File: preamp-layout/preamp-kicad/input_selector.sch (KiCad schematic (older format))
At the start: 43 parts, among them J50 Conn_01x02_Female, J51 Conn_01x03_Male, J52 Conn_01x03_Male, J53 Conn_01x03_Male, J54 Conn_01x03_Male, J55 Conn_01x03_Male, J56 Conn_01x07_Female, J57 Conn_01x07_Female, J58 Conn_01x03_Male, J59 Conn_01x03_Female, J60 Conn_01x02_Male, J61 Conn_01x02_Male, J62 Conn_01x03_Female, J63 Conn_01x03_Female, K2 G6JU, K3 G6JU, K4 G6JU, K5 G6JU, K6 G6JU, K7 G6JU, K8 G6JU, U6 MCP23017_SO, U7 ULN2003, U8 ULN2003

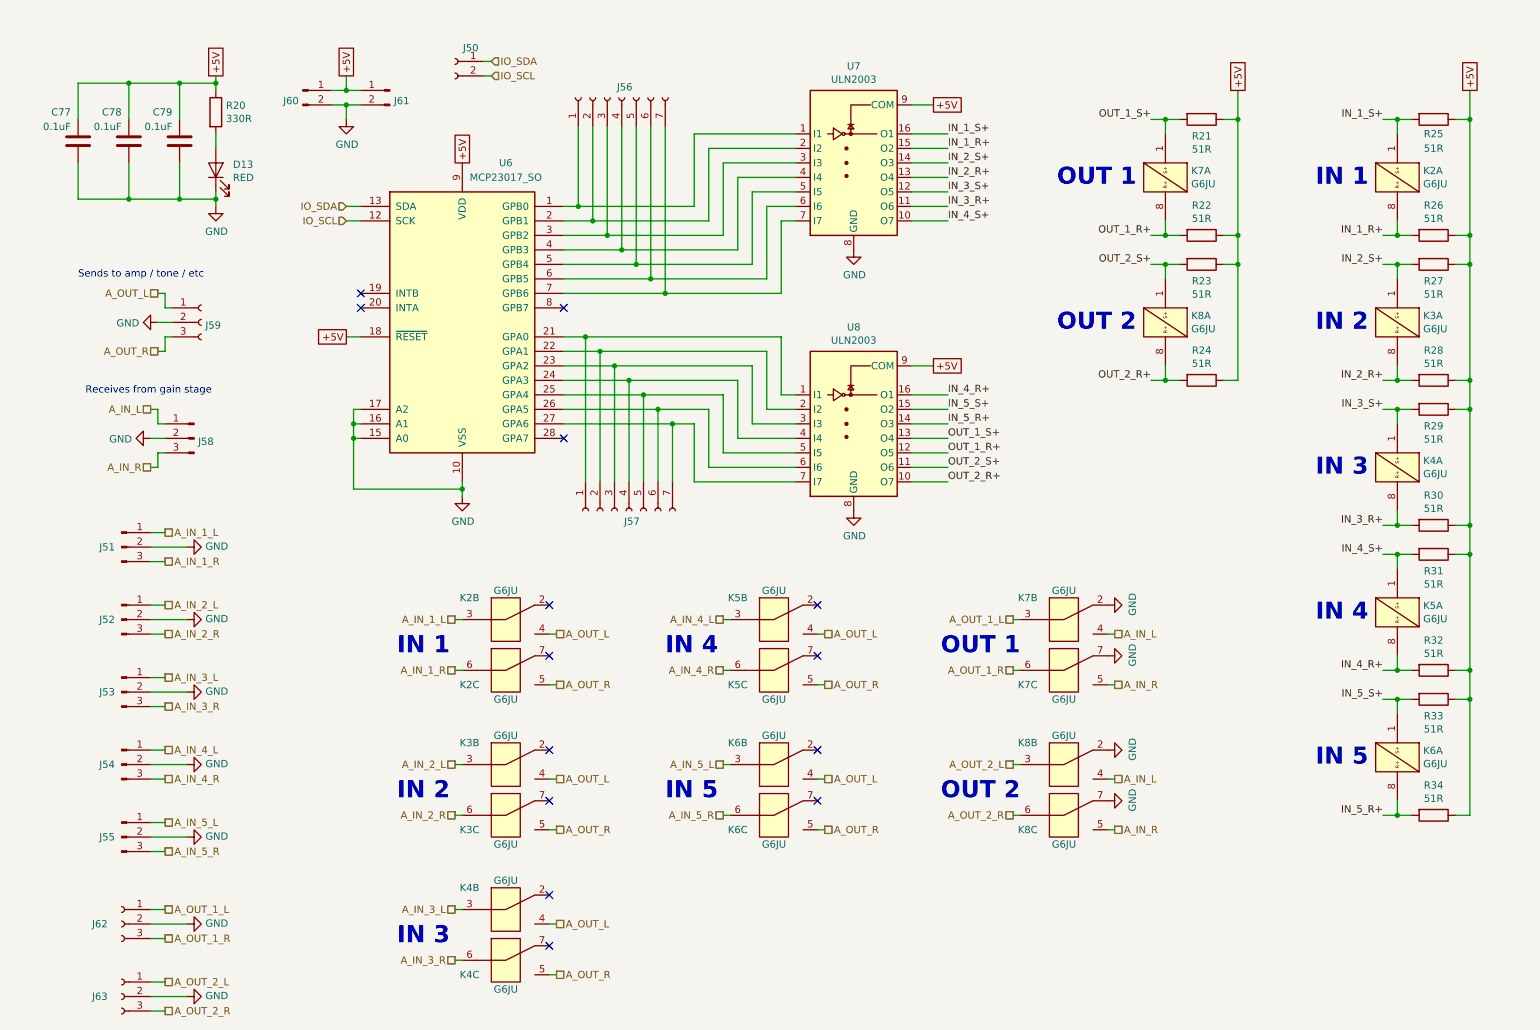
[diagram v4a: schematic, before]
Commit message: RefDes Update
Re-ran refdes assignment, updated BOM accordingly.
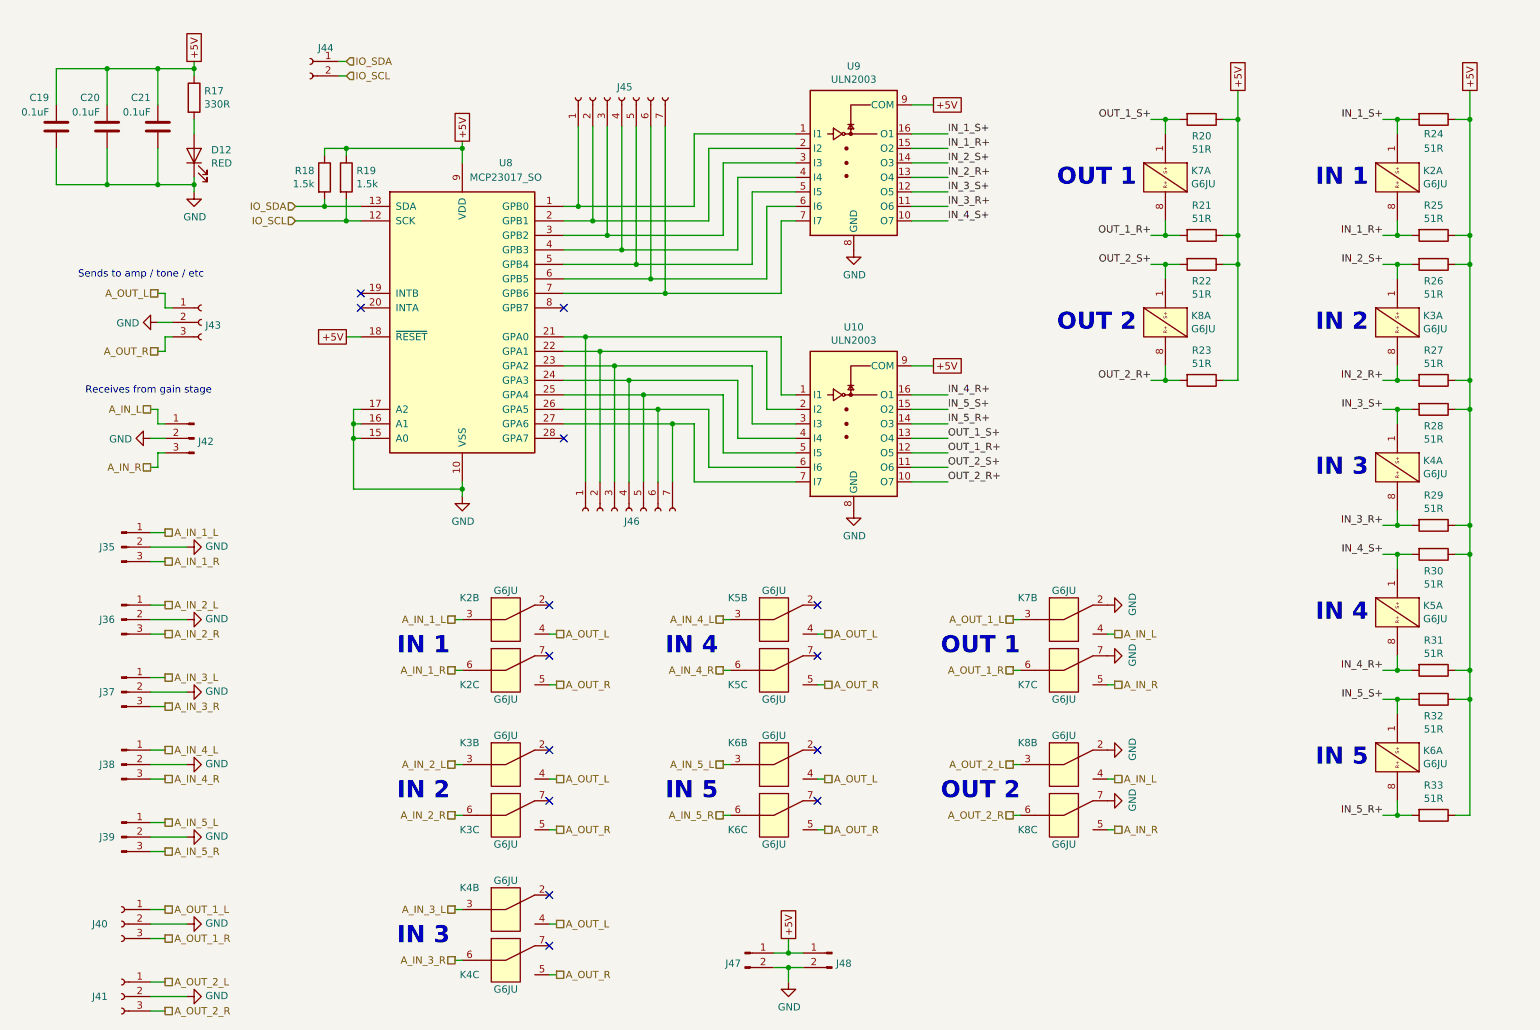
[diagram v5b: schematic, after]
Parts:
- added R18, R19: 1.5k, Resistor_SMD:R_1206_3216Metric_Pad1.42x1.75mm_HandSolder, symbol Device:R
- renumbered C77 to C19, C78 to C20, C79 to C21, D13 to D12, J51 to J35, J52 to J36, J53 to J37, J54 to J38, J55 to J39, J62 to J40, J63 to J41, J58 to J42, J59 to J43, J50 to J44, J56 to J45, J57 to J46, J60 to J47, J61 to J48, R20 to R17, R21 to R20, R22 to R21, R23 to R22, R24 to R23, R25 to R24, R26 to R25, R27 to R26, R28 to R27, R29 to R28, R30 to R29, R31 to R30, R32 to R31, R33 to R32, R34 to R33, U8 to U10, U6 to U8, U7 to U9
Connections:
- net +5V: now also R18.1, R19.1
- net IO_SCL: now also R19.2
- net IO_SDA: now also R18.2
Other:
- moved on the sheet: C19, C20, C21, D12, J44, J47, J48, R17

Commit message: Prelim PCB layout
Work done to lay out PCBs. Saving in anticipation of creating branch with a different input switching topology.
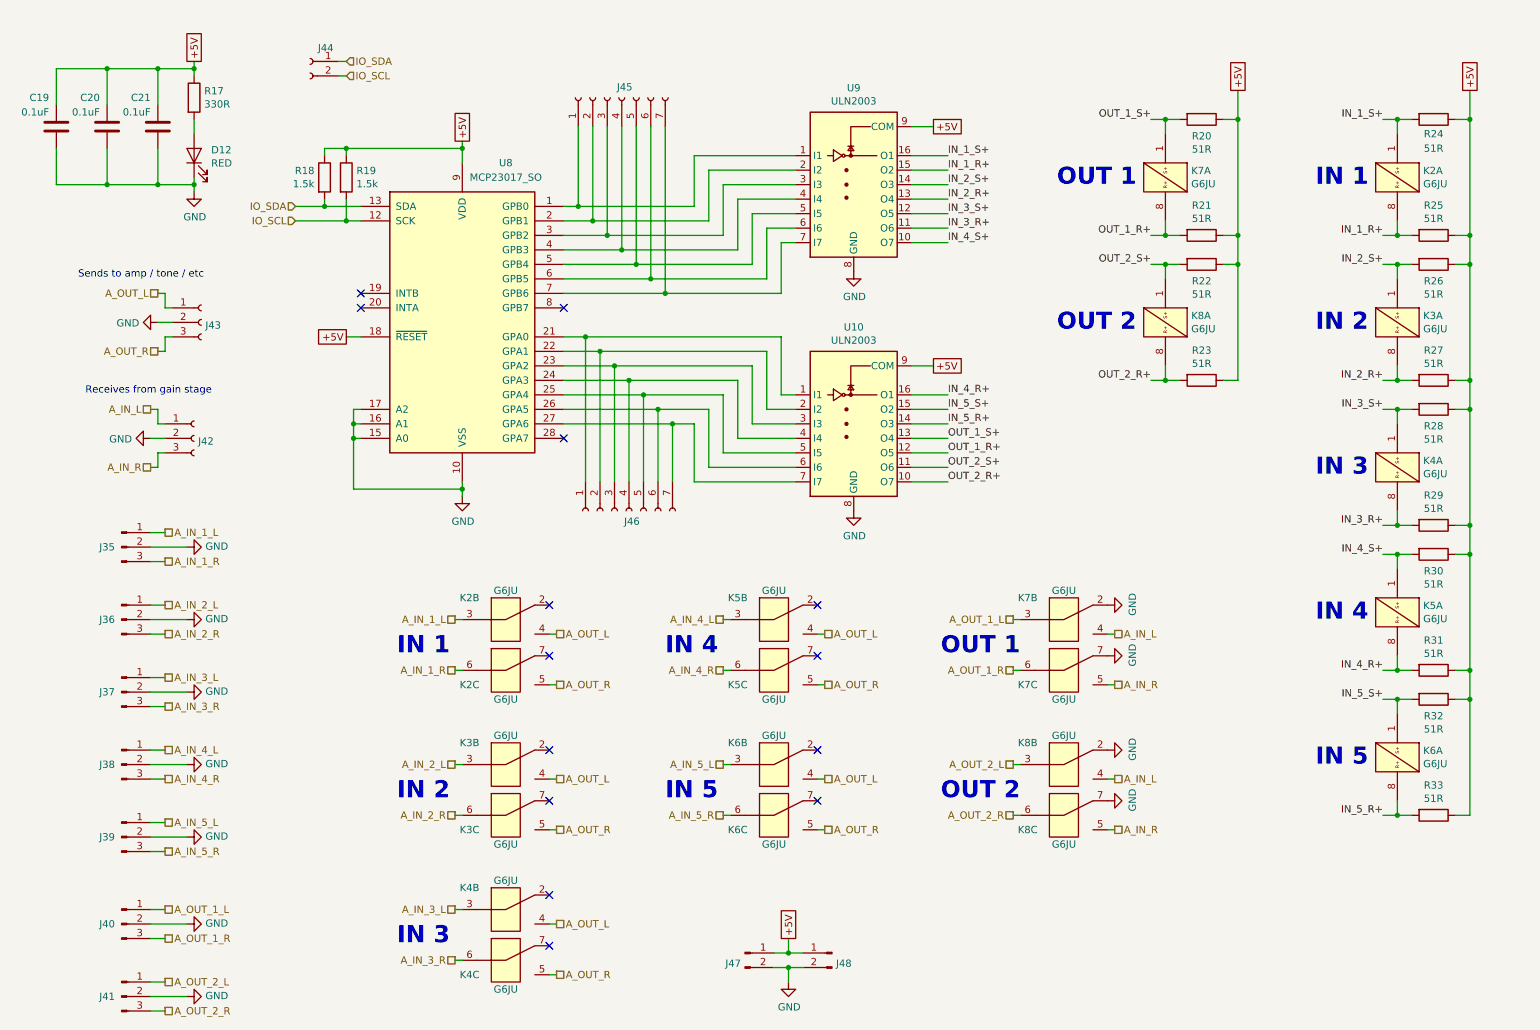
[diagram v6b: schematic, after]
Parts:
- removed J40, J41: Conn_01x03_Female, Connector_PinHeader_2.54mm:PinHeader_1x03_P2.54mm_Vertical, symbol Connector:Conn_01x03_Female
- removed J42: Conn_01x03_Male, Connector_PinHeader_2.54mm:PinHeader_1x03_P2.54mm_Vertical, symbol Connector:Conn_01x03_Male
- added J40, J41: Conn_01x03_Male, Connector_PinHeader_2.54mm:PinHeader_1x03_P2.54mm_Vertical, symbol Connector:Conn_01x03_Male
- added J42: Conn_01x03_Female, Connector_PinHeader_2.54mm:PinHeader_1x03_P2.54mm_Vertical, symbol Connector:Conn_01x03_Female
- J44: footprint (none) -> Connector_PinHeader_2.54mm:PinHeader_1x02_P2.54mm_Vertical
- J45, J46: footprint (none) -> Connector_PinHeader_2.54mm:PinHeader_1x07_P2.54mm_Vertical
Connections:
- net A_IN_L: now also J42.1 (Pin_1)
- net A_IN_R: now also J42.3 (Pin_3)
- net A_OUT_1_L: now also J40.1 (Pin_1)
- net A_OUT_1_R: now also J40.3 (Pin_3)
- net A_OUT_2_L: now also J41.1 (Pin_1)
- net A_OUT_2_R: now also J41.3 (Pin_3)
- net GND: now also J40.2 (Pin_2), J41.2 (Pin_2), J42.2 (Pin_2)
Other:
- moved on the sheet: U9
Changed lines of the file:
@@
 	1    0    0    -1
 $EndComp
-Text Label 7000 1400 0    50   ~ 0
-IN_1_S+
-Text GLabel 6900 1200 2    50   UnSpc ~ 0
-+5V
-Wire Wire Line
-	6900 1200 6750 1200
 Text GLabel 3650 1450 1    50   UnSpc ~ 0
 +5V
 Wire Wire Line
-	6750 1400 7000 1400
-Wire Wire Line
 	6750 3300 7000 3300
 Wire Wire Line
 	6750 3200 7000 3200
-Text Label 7000 2000 0    50   ~ 0
-IN_4_S+
 Text Label 7000 3200 0    50   ~ 0
 IN_4_R+
@@
 Text GLabel 2850 2800 0    50   UnSpc ~ 0
 +5V
-Text Label 7000 1900 0    50   ~ 0
-IN_3_R+
-Text Label 7000 1800 0    50   ~ 0
-IN_3_S+
-Wire Wire Line
-	6750 1800 7000 1800
-Wire Wire Line
-	6750 1900 7000 1900
-Wire Wire Line
-	6750 1700 7000 1700
-Wire Wire Line
-	6750 1600 7000 1600
-Wire Wire Line
-	6750 1500 7000 1500
-Text Label 7000 1600 0    50   ~ 0
-IN_2_S+
-Text Label 7000 1700 0    50   ~ 0
-IN_2_R+
-Text Label 7000 1500 0    50   ~ 0
-IN_1_R+
-$Comp
-L Transistor_Array:ULN2003 U9
-U 1 1 5E036B83
-P 6350 1600
-F 0 "U9" H 6350 2267 50  0000 C CNN
-F 1 "ULN2003" H 6350 2176 50  0000 C CNN
-F 2 "Package_SO:SOIC-16_3.9x9.9mm_P1.27mm" H 6400 1050 50  0001 L CNN
-F 3 "http://www.ti.com/lit/ds/symlink/uln2003a.pdf" H 6450 1400 50  0001 C CNN
-	1    6350 1600
-	1    0    0    -1
-$EndComp
 Wire Wire Line
 	3650 3900 3650 3850
@@
 	4350 3200 4900 3200
 Wire Wire Line
-	5750 2400 5750 1900
-Wire Wire Line
-	5650 2300 5650 1800
-Wire Wire Line
-	5550 2200 5550 1700
-Wire Wire Line
-	5450 2100 5450 1600
-Wire Wire Line
-	5350 2000 5350 1500
-Wire Wire Line
-	5250 1900 5250 1400
-Wire Wire Line
 	4500 3800 4500 2800
 Wire Wire Line
@@
 Wire Wire Line
 	5000 3800 5000 3300
-$Comp
-L Connector:Conn_01x03_Male J42
-U 1 1 637A81F9
-P 1800 3500
-F 0 "J42" H 1772 3478 50  0000 R CNN
-F 1 "Conn_01x03_Male" H 1772 3433 50  0001 R CNN
-F 2 "Connector_PinHeader_2.54mm:PinHeader_1x03_P2.54mm_Vertical" H 1800 3500 50  0001 C CNN
-F 3 "~" H 1800 3500 50  0001 C CNN
-	1    1800 3500
-	-1   0    0    -1
-$EndComp
 Text HLabel 1550 2900 0    50   UnSpc ~ 0
 A_OUT_R
@@
 OUT_2_S+
 Wire Wire Line
-	6750 2000 7000 2000
-Wire Wire Line
 	6750 3800 7000 3800
 $Comp
@@
 $EndComp
 Wire Wire Line
-	5250 1400 5950 1400
-Wire Wire Line
-	5350 1500 5950 1500
-Wire Wire Line
-	5450 1600 5950 1600
-Wire Wire Line
-	5550 1700 5950 1700
-Wire Wire Line
-	5650 1800 5950 1800
-Wire Wire Line
-	5750 1900 5950 1900
-Wire Wire Line
 	4350 2500 5050 2500
-Wire Wire Line
-	5850 2500 5850 2000
-Wire Wire Line
-	5850 2000 5950 2000
 Wire Wire Line
 	5850 2800 5850 3200
@@
 F 0 "J45" V 4823 1130 50  0000 C CNN
 F 1 "Conn_01x07_Female" V 4824 1130 50  0001 C CNN
-F 2 "" H 4750 1150 50  0001 C CNN
+F 2 "Connector_PinHeader_2.54mm:PinHeader_1x07_P2.54mm_Vertical" H 4750 1150 50  0001 C CNN
 F 3 "~" H 4750 1150 50  0001 C CNN
 	1    4750 1150
@@
 F 0 "J46" V 4873 3980 50  0000 C CNN
 F 1 "Conn_01x07_Female" V 4874 3980 50  0001 C CNN
-F 2 "" H 4800 4000 50  0001 C CNN
+F 2 "Connector_PinHeader_2.54mm:PinHeader_1x07_P2.54mm_Vertical" H 4800 4000 50  0001 C CNN
 F 3 "~" H 4800 4000 50  0001 C CNN
 	1    4800 4000
@@
 Wire Wire Line
 	1500 7350 1750 7350
-$Comp
-L Connector:Conn_01x03_Female J?
-U 1 1 63BC6293
-P 1300 7350
-AR Path="/5E607732/63BC6293" Ref="J?"  Part="1"
-AR Path="/5E2D8DA2/63BC6293" Ref="J41"  Part="1"
-F 0 "J41" H 1450 7350 50  0000 C CNN
-F 1 "Conn_01x03_Female" H 1328 7285 50  0001 L CNN
-F 2 "Connector_PinHeader_2.54mm:PinHeader_1x03_P2.54mm_Vertical" H 1300 7350 50  0001 C CNN
-F 3 "~" H 1300 7350 50  0001 C CNN
-	1    1300 7350
-	-1   0    0    -1
-$EndComp
 Text Notes 6950 6000 0    118  ~ 24
 OUT 2
@@
 Text HLabel 7450 6100 0    50   UnSpc ~ 0
 A_OUT_2_R
-$Comp
-L Connector:Conn_01x03_Female J?
-U 1 1 620969B0
-P 1300 6850
-AR Path="/5E607732/620969B0" Ref="J?"  Part="1"
-AR Path="/5E2D8DA2/620969B0" Ref="J40"  Part="1"
-F 0 "J40" H 1450 6850 50  0000 C CNN
-F 1 "Conn_01x03_Female" H 1328 6785 50  0001 L CNN
-F 2 "Connector_PinHeader_2.54mm:PinHeader_1x03_P2.54mm_Vertical" H 1300 6850 50  0001 C CNN
-F 3 "~" H 1300 6850 50  0001 C CNN
-	1    1300 6850
-	-1   0    0    -1
-$EndComp
 Text Notes 6950 5000 0    118  ~ 24
 OUT 1
@@
 F 3 "" H 3650 3900 50  0001 C CNN
 	1    3650 3900
-	1    0    0    -1
-$EndComp
-$Comp
-L power:GND #PWR?
-U 1 1 64C160A3
-P 6350 2200
-AR Path="/5E26F6FE/64C160A3" Ref="#PWR?"  Part="1"
-AR Path="/5E2D8DA2/64C160A3" Ref="#PWR053"  Part="1"
-F 0 "#PWR053" H 6350 1950 50  0001 C CNN
-F 1 "GND" H 6355 2027 50  0000 C CNN
-F 2 "" H 6350 2200 50  0001 C CNN
-F 3 "" H 6350 2200 50  0001 C CNN
-	1    6350 2200
 	1    0    0    -1
 $EndComp
@@
 F 0 "J44" H 2492 993 50  0000 C CNN
 F 1 "Conn_01x02_Female" H 2492 994 50  0001 C CNN
-F 2 "" H 2600 900 50  0001 C CNN
+F 2 "Connector_PinHeader_2.54mm:PinHeader_1x02_P2.54mm_Vertical" H 2600 900 50  0001 C CNN
 F 3 "~" H 2600 900 50  0001 C CNN
 	1    2600 900
@@
 Wire Wire Line
 	2700 1900 2950 1900
+Wire Wire Line
+	5850 2500 5850 2150
+Wire Wire Line
+	5750 2400 5750 2050
+Wire Wire Line
+	5650 2300 5650 1950
+Wire Wire Line
+	5550 2200 5550 1850
+Wire Wire Line
+	5450 2100 5450 1750
+Wire Wire Line
+	5350 2000 5350 1650
+Wire Wire Line
+	5250 1900 5250 1550
+$Comp
+L power:GND #PWR?
+U 1 1 64C160A3
+P 6350 2350
+AR Path="/5E26F6FE/64C160A3" Ref="#PWR?"  Part="1"
+AR Path="/5E2D8DA2/64C160A3" Ref="#PWR053"  Part="1"
+F 0 "#PWR053" H 6350 2100 50  0001 C CNN
+F 1 "GND" H 6355 2177 50  0000 C CNN
+F 2 "" H 6350 2350 50  0001 C CNN
+F 3 "" H 6350 2350 50  0001 C CNN
+	1    6350 2350
+	1    0    0    -1
+$EndComp
+Wire Wire Line
+	5850 2150 5950 2150
+Wire Wire Line
+	5750 2050 5950 2050
+Wire Wire Line
+	5650 1950 5950 1950
+Wire Wire Line
+	5550 1850 5950 1850
+Wire Wire Line
+	5450 1750 5950 1750
+Wire Wire Line
+	5350 1650 5950 1650
+Wire Wire Line
+	5250 1550 5950 1550
+Wire Wire Line
+	6750 2150 7000 2150
+$Comp
+L Transistor_Array:ULN2003 U9
+U 1 1 5E036B83
+P 6350 1750
+F 0 "U9" H 6350 2417 50  0000 C CNN
+F 1 "ULN2003" H 6350 2326 50  0000 C CNN
+F 2 "Package_SO:SOIC-16_3.9x9.9mm_P1.27mm" H 6400 1200 50  0001 L CNN
+F 3 "http://www.ti.com/lit/ds/symlink/uln2003a.pdf" H 6450 1550 50  0001 C CNN
+	1    6350 1750
+	1    0    0    -1
+$EndComp
+Text Label 7000 1650 0    50   ~ 0
+IN_1_R+
+Text Label 7000 1850 0    50   ~ 0
+IN_2_R+
+Text Label 7000 1750 0    50   ~ 0
+IN_2_S+
+Wire Wire Line
+	6750 1650 7000 1650
+Wire Wire Line
+	6750 1750 7000 1750
+Wire Wire Line
+	6750 1850 7000 1850
+Wire Wire Line
+	6750 2050 7000 2050
+Wire Wire Line
+	6750 1950 7000 1950
+Text Label 7000 1950 0    50   ~ 0
+IN_3_S+
+Text Label 7000 2050 0    50   ~ 0
+IN_3_R+
+Text Label 7000 2150 0    50   ~ 0
+IN_4_S+
+Wire Wire Line
+	6750 1550 7000 1550
+Wire Wire Line
+	6900 1350 6750 1350
+Text GLabel 6900 1350 2    50   UnSpc ~ 0
++5V
+Text Label 7000 1550 0    50   ~ 0
+IN_1_S+
+$Comp
+L Connector:Conn_01x03_Female J?
+U 1 1 61432578
+P 1800 3500
+AR Path="/5E607732/61432578" Ref="J?"  Part="1"
+AR Path="/5E2D8DA2/61432578" Ref="J42"  Part="1"
+F 0 "J42" H 1828 3480 50  0000 L CNN
+F 1 "Conn_01x03_Female" H 1828 3435 50  0001 L CNN
+F 2 "Connector_PinHeader_2.54mm:PinHeader_1x03_P2.54mm_Vertical" H 1800 3500 50  0001 C CNN
+F 3 "~" H 1800 3500 50  0001 C CNN
+	1    1800 3500
+	1    0    0    -1
+$EndComp
+$Comp
+L Connector:Conn_01x03_Male J40
+U 1 1 61461D5D
+P 1300 6850
+F 0 "J40" H 1200 6850 50  0000 C CNN
+F 1 "Conn_01x03_Male" H 1272 6783 50  0001 R CNN
+F 2 "Connector_PinHeader_2.54mm:PinHeader_1x03_P2.54mm_Vertical" H 1300 6850 50  0001 C CNN
+F 3 "~" H 1300 6850 50  0001 C CNN
+	1    1300 6850
+	1    0    0    -1
+$EndComp
+$Comp
+L Connector:Conn_01x03_Male J41
+U 1 1 61461D67
+P 1300 7350
+F 0 "J41" H 1200 7350 50  0000 C CNN
+F 1 "Conn_01x03_Male" H 1272 7283 50  0001 R CNN
+F 2 "Connector_PinHeader_2.54mm:PinHeader_1x03_P2.54mm_Vertical" H 1300 7350 50  0001 C CNN
+F 3 "~" H 1300 7350 50  0001 C CNN
+	1    1300 7350
+	1    0    0    -1
+$EndComp
 $EndSCHEMATC
